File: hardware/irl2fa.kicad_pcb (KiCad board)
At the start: 2 copper layers, 77 x 31 mm, 52 parts, among them J1 FH34SRJ-24S, J3 TC2030-NL, Q1 AO3401A, Q2 AO3401A, Q3 Si1308EDL, Q4 AO3400A, Q5 VEMT2523SLX01, SW1 SKRHABE010, U1 STM32U083KCU6, U2 RV-3032-C7

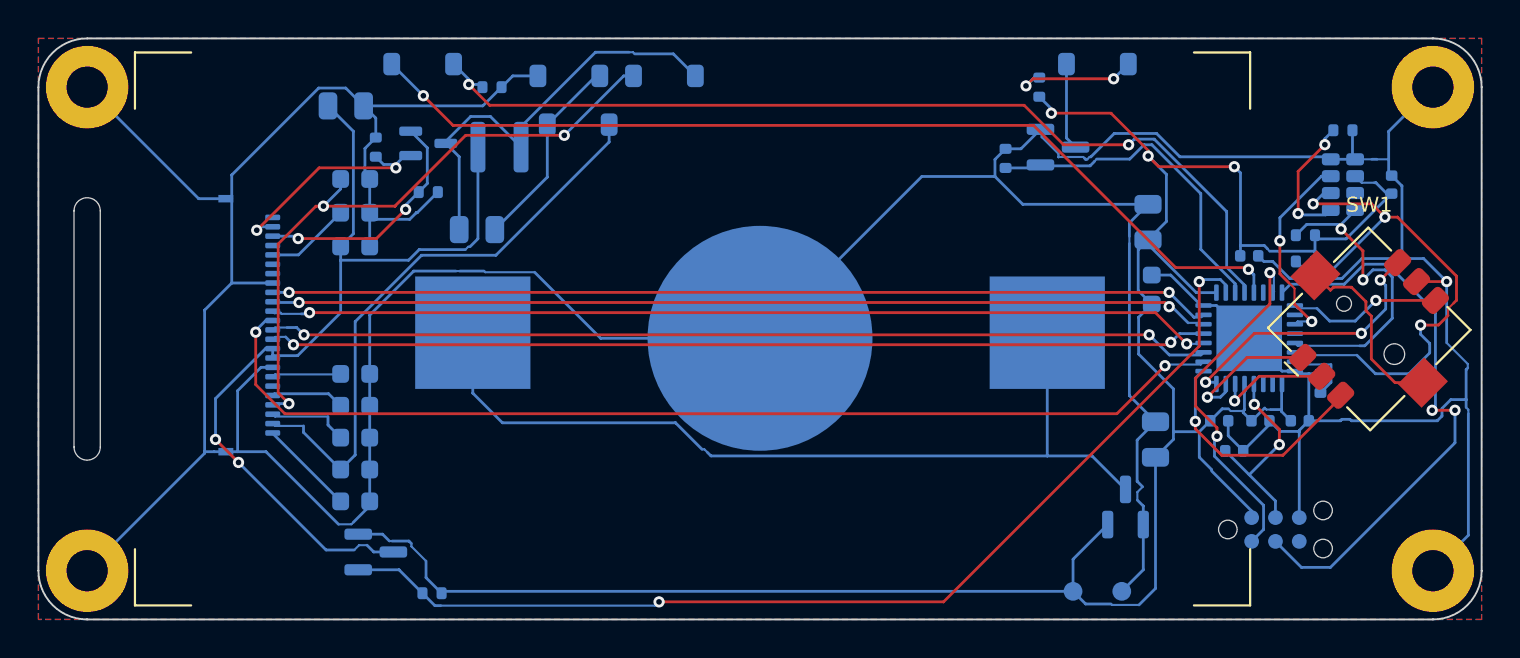
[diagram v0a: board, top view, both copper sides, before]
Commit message: Apply the review fixes to the board and re-route it
Mechanical review:
- MECH-01: FPC slot 1.4 x 17.0 mm (y 6.3..23.3) so it covers the flex's
  14.3 mm flare; EPD footprint, board, case dims and fab outputs regenerated.
- MECH-04: B.Cu ring under the cell's negative cap (r 6..10.5) with no
  tracks or pour except one 1.2 mm corridor straight down; the pad's GND
  spoke runs through it with the solder mask open, so it is bare like the
  pad. Pad 2 joins the pour solid. New test checks tracks and pour.
- MECH-05: no vias in the cell's insertion path (x 25.9..51.1 to the
  bottom edge); cell via keep-out r 12.6.
- MECH-09: board.yaml carries the keytop stem data; the .scad reads it.

Electrical review:
- IR-1: Q5 -> VEMT2023SLX01 (C2843576, daylight filter, same drawing and
  lead order); footprint renamed; JLC correction 180 (EasyEDA draws it
  turned against the VEMT2523SLX01) with its pads in jlc_footprints.yaml.
- IR-2: R8 68 ohm (C25131; no Basic 68 ohm 0402 exists); ir_led limit
  0.035 A, ir_rx checks 3 cm (worst-case range now ~3.5 cm), new
  ir_burst.cir checks the cell during a 90 % duty transmit burst; power
  model 25 / 35 mA.
- EPD-1: Q3 -> NX3008NBK,215 (C179399, SOT-23, Vgs(th) 1.1 V max) at the
  old Q3 spot; booster bench models it at its worst-case Vth/Rds(on).
- C-1, C-2: L1 "0.36 A"; D4 and Q5 datasheet links.
- C-5: SW1 frame tabs to GND.

Assembly review:
- A-07: silkscreen 1.0 mm / 0.153 mm; refs with no room are hidden.
- A-08 / A-12: /GND pours; Power class on the supply nets (0.3 / 0.2 mm),
  GND in a Ground class (0.3 / 0.15 mm): with 0.2 mm round every ground
  pad Freerouting left 26-38 connections unrouted.
- A-10: clip legs' paste reduced to ~78 %.

Factory programming: TP1-TP5 (GND, VBAT, SWDIO, SWCLK, NRST), 1.5 mm pads
on a 2.54 mm grid along the bottom edge on the back, labelled; README
"Build one" describes JLCPCB's programming option. TC2030 J3 kept.

ERC 0, DRC 0 with 0 unconnected; make hardware / case / firmware pass.

Co-Author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
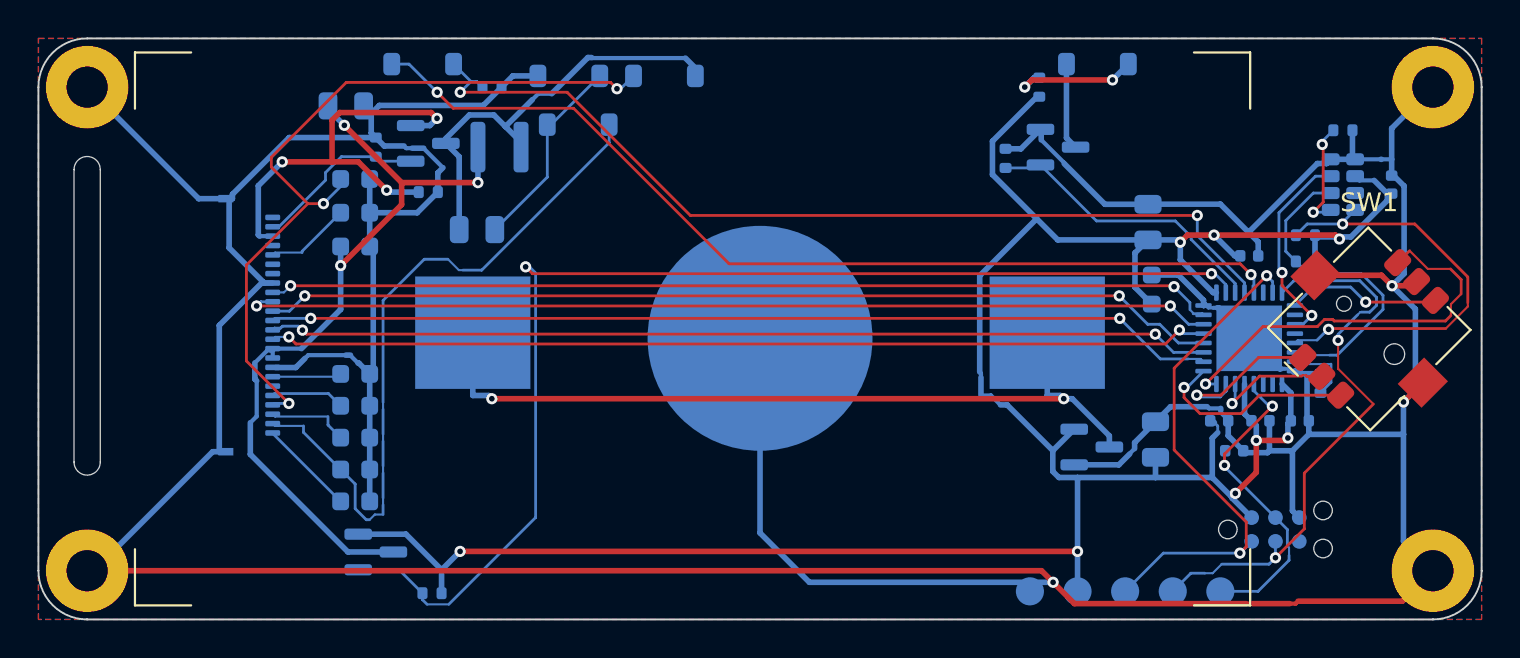
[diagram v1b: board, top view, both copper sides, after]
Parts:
- added TP3: SWDIO, TestPoint:TestPoint_Pad_D1.5mm, B.Cu at (158.0, 129.5)
- added TP4: SWCLK, TestPoint:TestPoint_Pad_D1.5mm, B.Cu at (160.5, 129.5)
- added TP5: NRST, TestPoint:TestPoint_Pad_D1.5mm, B.Cu at (163.1, 129.5)
- Q3: value Si1308EDL -> NX3008NBK; footprint Package_TO_SOT_SMD:SOT-323_SC-70 -> Package_TO_SOT_SMD:SOT-23
- Q5: value VEMT2523SLX01 -> VEMT2023SLX01; footprint irl2fa:PhotoTransistor_Vishay_VEMT2523SLX01_SideView -> irl2fa:PhotoTransistor_Vishay_VEMT2023SLX01_SideView
- R8: value 100 -> 68
- TP1, TP2: footprint TestPoint:TestPoint_Pad_D1.0mm -> TestPoint:TestPoint_Pad_D1.5mm
- moved TP2 4.90 mm to (152.9, 129.5)
- moved Q1 3.67 mm to (156.2, 121.8), turned to 0 degrees
- moved TP1 0.24 mm to (155.4, 129.5)
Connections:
- SW1 pad MP: unconnected-(SW1-PadMP) -> /GND
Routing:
- net /GND: track 266.9 -> 296.1 mm, vias 1 -> 3
- net /I2C_SDA: track 30.4 -> 17.3 mm, vias 3 -> 0
- net /VBAT: track 126.7 -> 137.2 mm, vias 3 -> 8
- net /EPD_RESE: track 12.8 -> 22.9 mm, vias 2 -> 3
- net unconnected-(SW1-PadMP): track 9.85 -> 0.00 mm
- net /SWDIO: track 19.0 -> 27.5 mm
- net /EPD_PWR_N: track 56.8 -> 64.2 mm
- net /EPD_PREVGH: track 34.2 -> 41.1 mm
- net /JOY_B: track 14.8 -> 21.7 mm, vias 3 -> 1
- net /NRST: track 10.7 -> 17.5 mm
- net /VEPD: track 48.2 -> 41.9 mm, vias 2 -> 3
- net /I2C_SCL: track 17.2 -> 23.2 mm
- net /EPD_PREVGL: track 31.5 -> 37.5 mm
- net /EPD_CS: track 56.4 -> 50.7 mm
- net /VBAT_RAW: track 46.8 -> 43.1 mm, vias 0 -> 2
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- added copper zone on B.Cu, net /GND
- added copper zone on F.Cu, net /GND
- removed copper zone on B.Cu, net (none)
- removed copper zone on F.Cu, net (none)
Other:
- board text added: "CLK"
- board text added: "DIO"
- board text added: "GND"
- board text added: "RST"
- board text added: "VBAT"

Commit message: Release v0.2.0: version bump, board revision mark, release notes
- IRL2FA_VERSION 0.2.0; silkscreen "v0.2  irl2fa.com"; fab outputs, renders
  and screen images regenerated.
- gen_pcb.py --step silk: a marking whose wording changed is reused for the
  new text (pcbnew can't remove it from Python), and the list of unwanted
  texts is built before the test-pad labels are placed, so a fresh board
  build no longer hits an undefined name.
- Release notes for v0.2.0.

Co-Authored-By: Claude Opus 5.5 <noreply@anthropic.com>
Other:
- board text added: "v0.2 irl2fa.com"
- board text removed: "v0.1 irl2fa.com"
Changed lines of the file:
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@@
 		(tags "Vishay VEMT2023SLX01 side looking side view MiniLED infrared")
 		(property "Reference" "Q5"
-			(at -6.1745 -4.978515 0)
+			(at -6.1745 -4.978514 0)
 			(layer "B.SilkS")
 			(hide yes)
@@
 		(tags "wirewound power shielded")
 		(property "Reference" "L1"
-			(at 5.505452 5.298515 0)
+			(at 5.505452 5.298514 0)
 			(layer "B.SilkS")
 			(hide yes)
@@
 		(tags "capacitor")
 		(property "Reference" "C12"
-			(at -5.756881 -4.278515 0)
+			(at -5.756881 -4.278516 0)
 			(layer "B.SilkS")
 			(effects
@@
 		)
 	)
-	(gr_text "v0.1  irl2fa.com"
+	(gr_text "v0.2  irl2fa.com"
 		(at 142.5 101.9 0)
 		(layer "B.SilkS")
